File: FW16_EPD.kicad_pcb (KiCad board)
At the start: 2 copper layers, 67.8 x 132 mm, 62 parts, among them J1 Conn_01x02, J2 Framework Input Module Connec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, J3 FH34SRJ-24S-0.5SH, J4 FH34SRJ-6S-0.5SH, Q1 DMG3404L, Q2 SSM3J338R, U1 RP2040, U2 W25Q128JVP, U3 MCP9808_DFN, Y1 12.000 MHz ABM8-272-T3

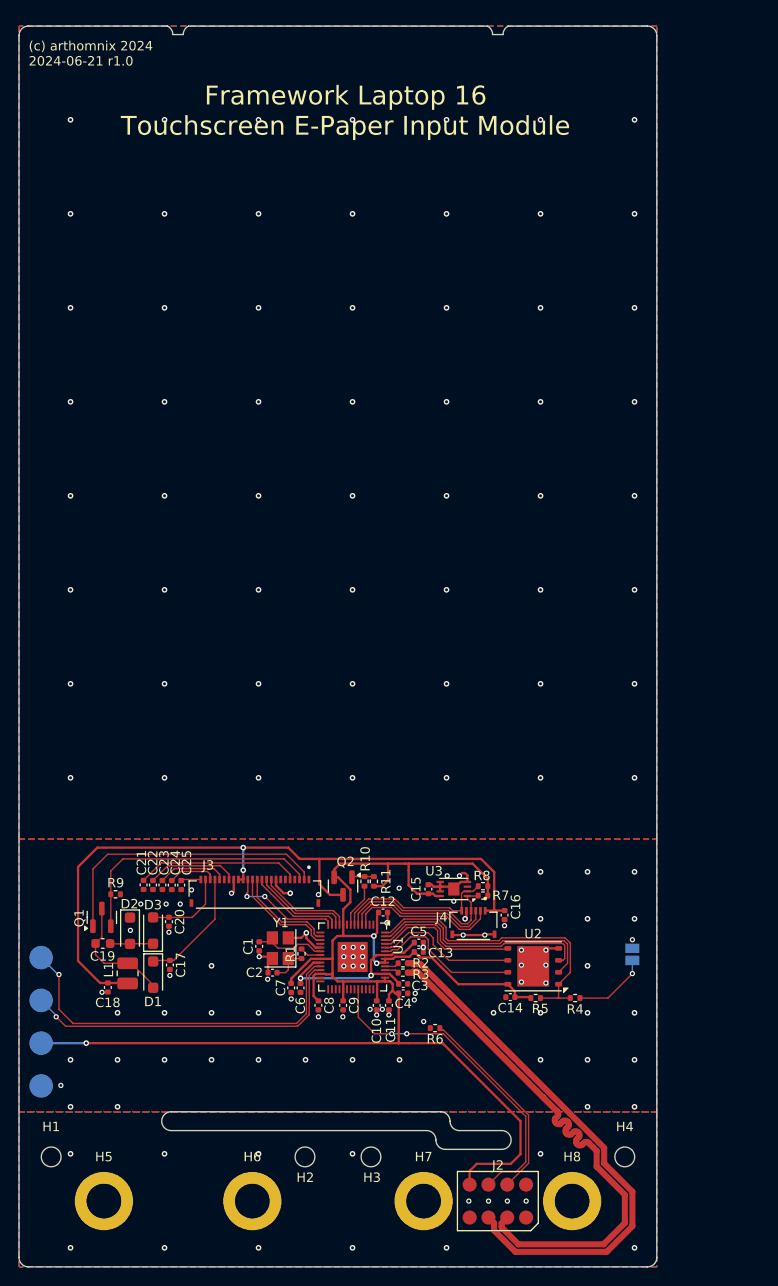
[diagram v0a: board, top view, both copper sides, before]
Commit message: pcb: add CC and OSHW symbols; silkscreen rearrangements
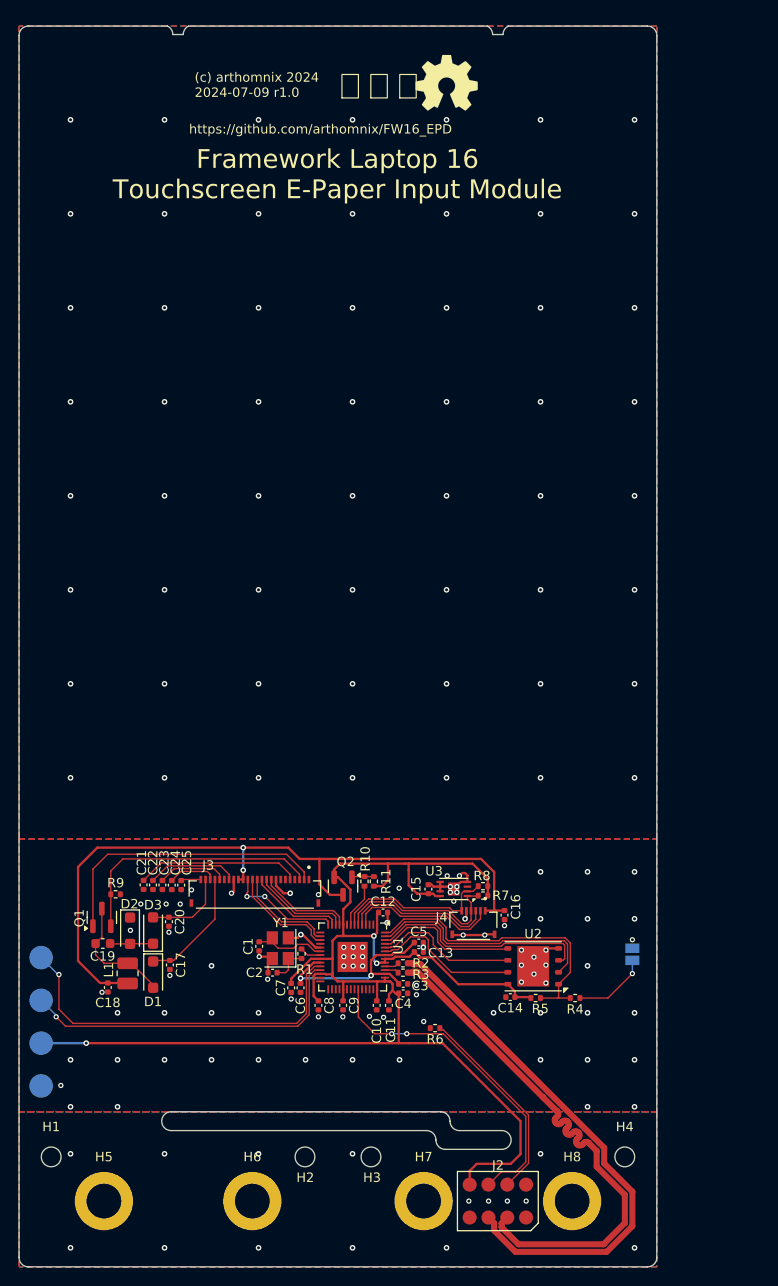
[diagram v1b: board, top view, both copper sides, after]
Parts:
- added REF**: OSHW-Symbol_6.7x6mm_SilkScreen, Symbol:OSHW-Symbol_6.7x6mm_SilkScreen, F.Cu at (137.8, 37.8)
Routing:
- net GND: track 32.9 -> 32.6 mm, vias 153 -> 157
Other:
- board text added: "(c) arthomnix 2024 2024-07-09 r1.0"
- board text added: "https://github.com/arthomnix/FW16_EPD"
- board text added: "🅭 🅯 🄎"
- board text removed: "(c) arthomnix 2024 2024-06-21 r1.0"

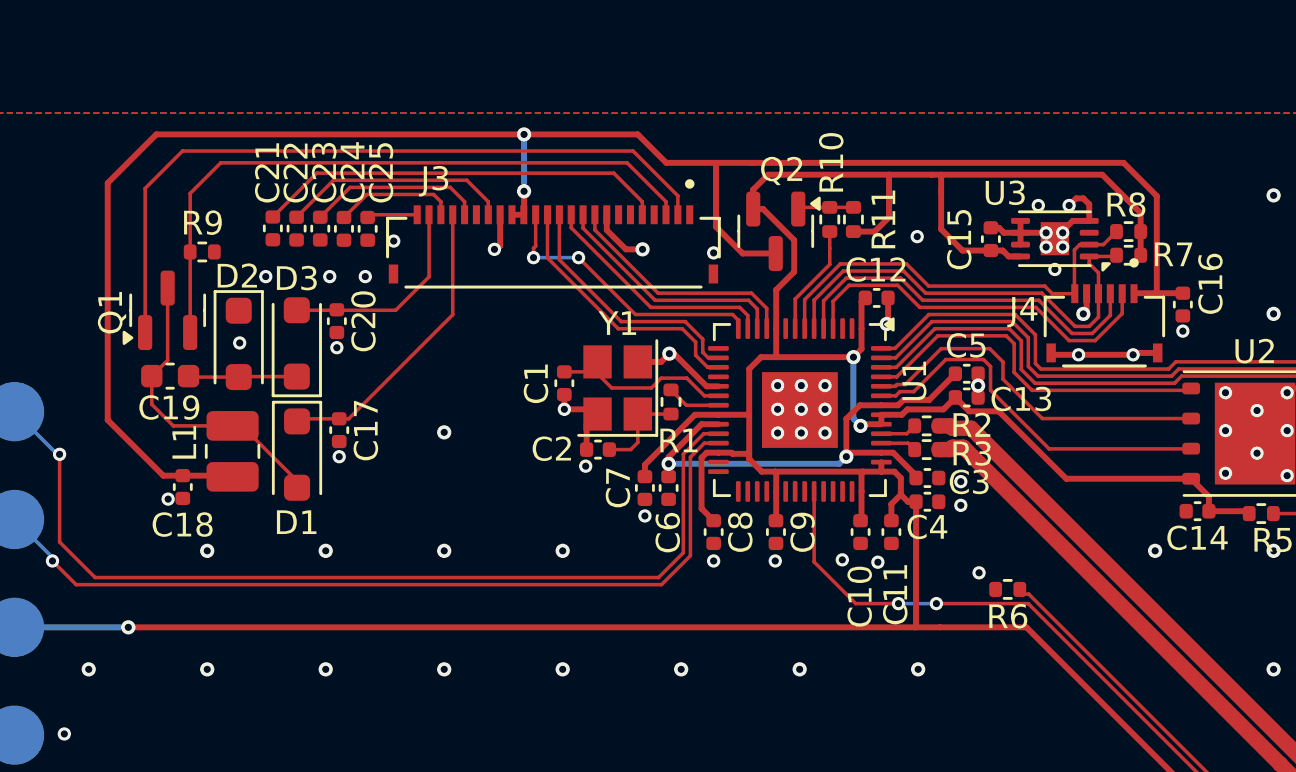
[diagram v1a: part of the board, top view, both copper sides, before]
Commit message: sch/pcb: add TVS diodes; thicker traces for EPD DC/DC
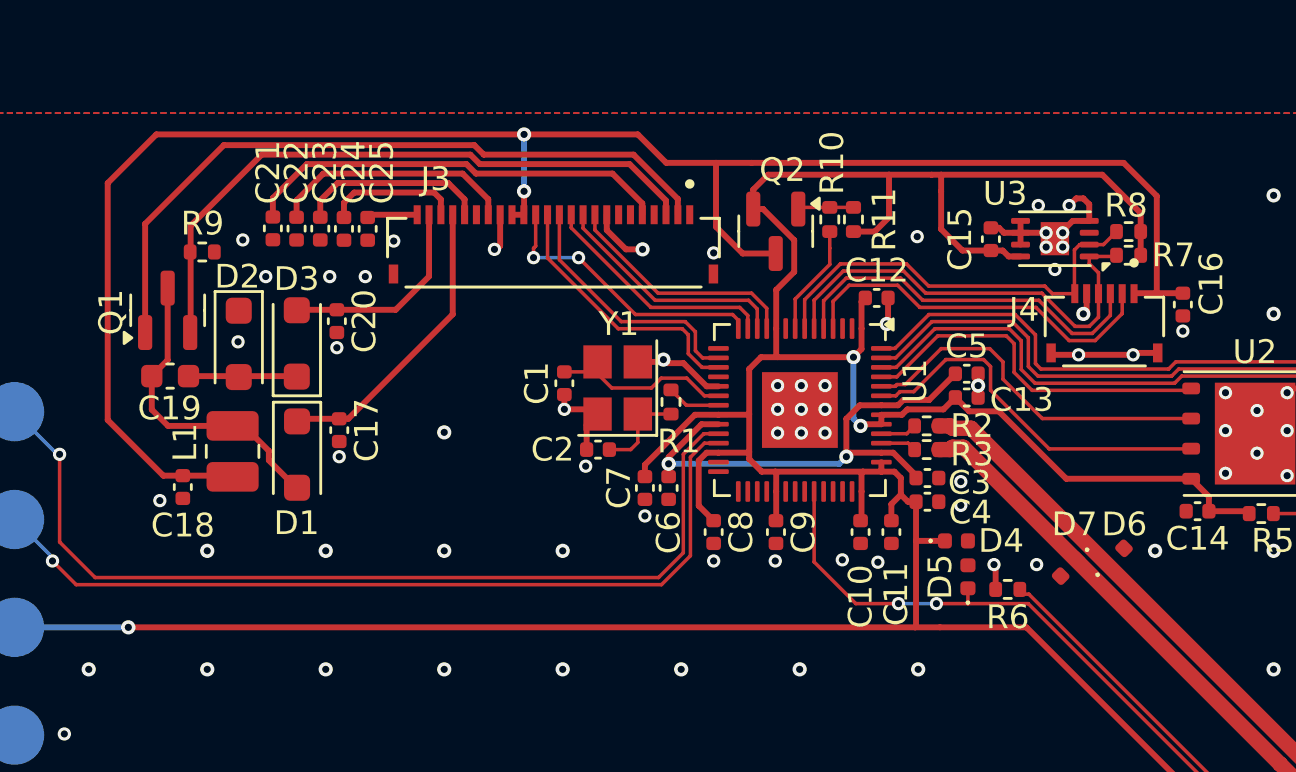
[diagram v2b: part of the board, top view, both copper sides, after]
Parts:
- added D4: SP0402B-ULC-01ETG, Diode_SMD:D_0402_1005Metric, F.Cu at (134.4, 136.3)
- added D5: SP0402B-ULC-01ETG, Diode_SMD:D_0402_1005Metric, F.Cu at (134.9, 137.8)
- added D6: SP0402B-ULC-01ETG, Diode_SMD:D_0402_1005Metric, F.Cu at (141.1, 137.0)
- added D7: SP0402B-ULC-01ETG, Diode_SMD:D_0402_1005Metric, F.Cu at (139.2, 137.4)
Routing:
- net +3V3: track 166.5 -> 167.8 mm
- net GND: track 32.6 -> 33.4 mm, vias 157 -> 159
- net /EPD_GDR: track 30.8 -> 30.0 mm
- net /EPD_VDHR: track 17.4 -> 18.1 mm
- net /EPD_VDDD: track 9.66 -> 10.4 mm
- net /SLEEP#: track 35.4 -> 36.1 mm
- net /EPD_VDH: track 7.41 -> 8.04 mm

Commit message: pcb: update dates
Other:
- board text added: "(c) arthomnix 2024 2024-07-10 r1.0"
- board text added: "FW16_EPD r1.0 2024-07-10 (c) arthomnix 2024"
- board text removed: "(c) arthomnix 2024 2024-07-09 r1.0"
- board text removed: "FW16_EPD r1.0 2024-06-21 (c) arthomnix 2024"
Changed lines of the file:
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@@
 		)
 	)
-	(gr_text "FW16_EPD r1.0 2024-06-21 (c) arthomnix 2024"
-		(at 94.25 109.59 -90)
+	(gr_text "FW16_EPD r1.0 2024-07-10 (c) arthomnix 2024"
+		(at 94.25 109.59 270)
 		(layer "B.SilkS")
 		(effects
@@
 		)
 	)
-	(gr_text "(c) arthomnix 2024\n2024-07-09 r1.0"
+	(gr_text "(c) arthomnix 2024\n2024-07-10 r1.0"
 		(at 111 39.4 0)
 		(layer "F.SilkS")

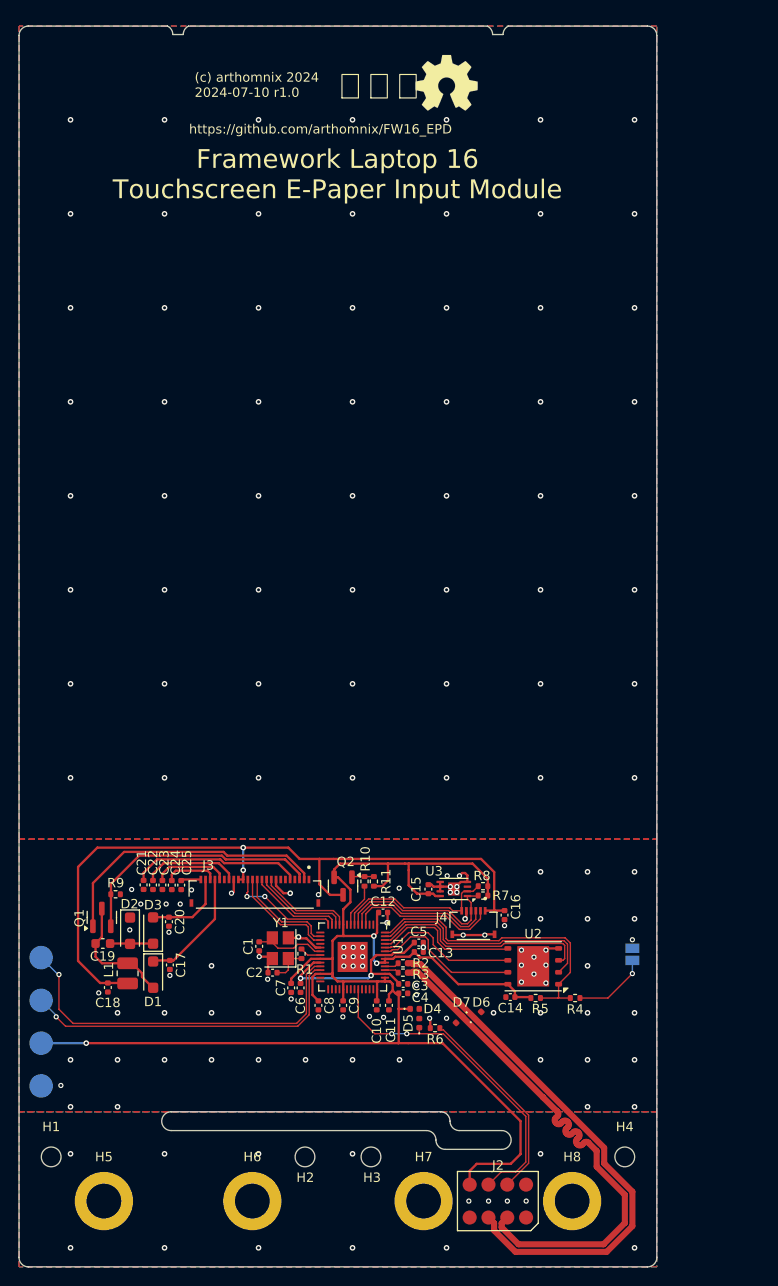
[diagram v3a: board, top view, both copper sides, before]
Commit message: pcb: measurements corrections
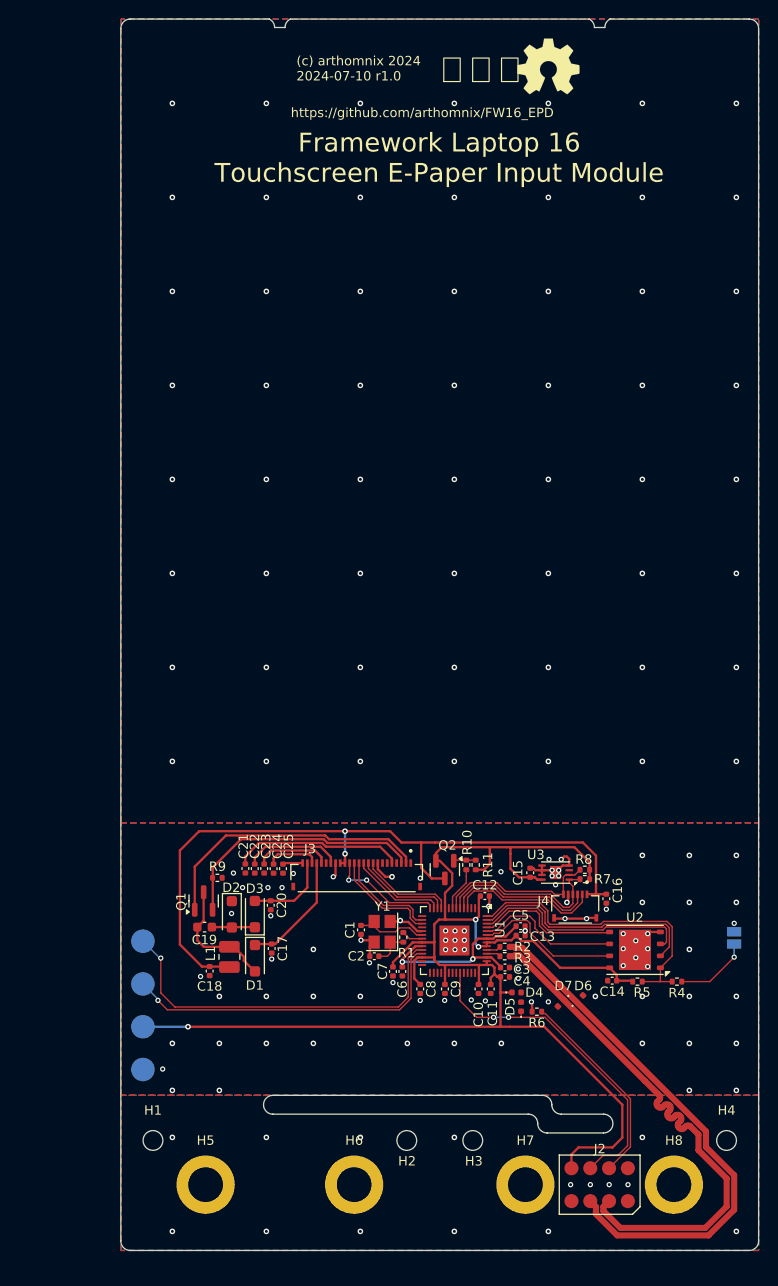
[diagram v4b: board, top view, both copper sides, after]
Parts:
- moved C13 11.0 mm to (145.7, 128.5)
- moved C5 11.0 mm to (145.7, 127.5)
- moved D4 11.0 mm to (145.2, 134.6)
- moved D6 11.0 mm to (152.0, 135.2)
- moved D7 11.0 mm to (150.0, 135.7)
- moved H8 11.0 mm to (162.0, 155.0)
- moved J1 11.0 mm to (168.4, 128.8)
- moved J2 11.0 mm to (154.1, 155.0)
- moved R2 11.0 mm to (144.0, 129.7)
- moved R3 11.0 mm to (144.0, 130.7)
- moved C16 11.0 mm to (154.8, 124.6)
- moved C21 11.0 mm to (116.4, 121.4)
- moved C22 11.0 mm to (117.4, 121.4)
- moved C23 11.0 mm to (118.4, 121.4)
- moved C24 11.0 mm to (119.4, 121.4)
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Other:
- board size 67.8 x 132 mm -> 67.8 x 131 mm
